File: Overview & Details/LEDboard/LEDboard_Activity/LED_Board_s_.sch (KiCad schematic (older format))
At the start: 6 parts, among them J1 Conn_01x04

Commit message: Create LEDboard schematic
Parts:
- added D10, D11, D12, D13, D14, D15, D16, D17, D18, D19, D2, D20, D21, D22, D23, D24, D25, D26, D27, D28, D29, D3, D30, D31, D32, D33, D34, D35, D36, D37, D38, D39, D4, D40, D41, D42, D43, D44, D45, D46, D47, D48, D5, D6, D7, D8, D9: APA102-2020, LED_SMD:LED-APA102-2020, symbol LED:APA102-2020
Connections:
- wire segments 9 -> 125
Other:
- note added: "NC"
- note removed: "n/c"

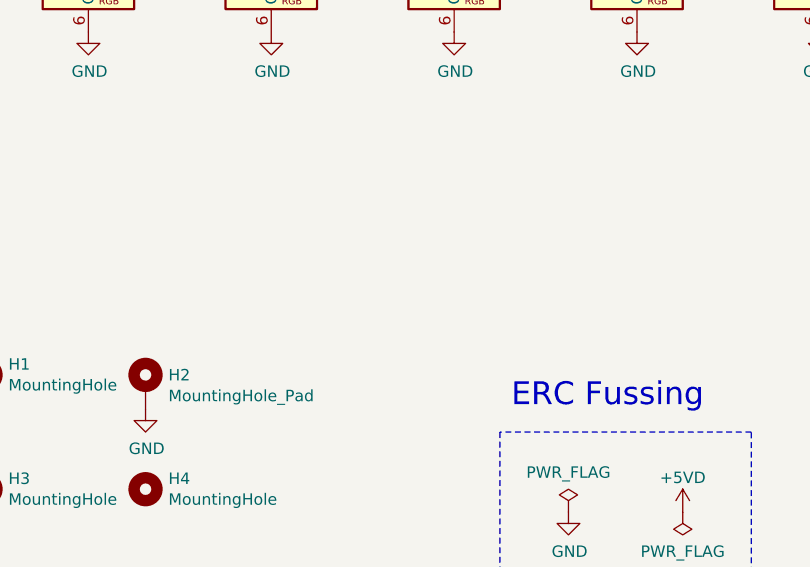
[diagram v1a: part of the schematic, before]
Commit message: add fiducials
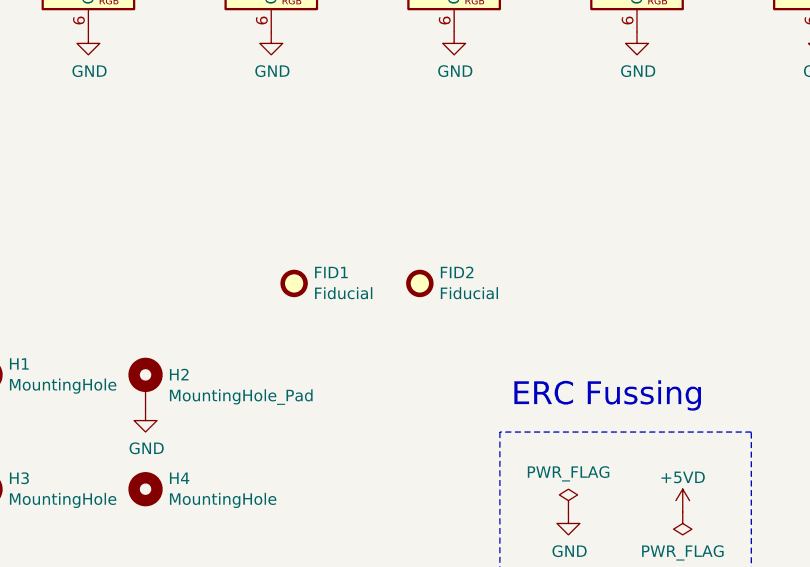
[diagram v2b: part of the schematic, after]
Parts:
- added FID1, FID2: Fiducial, Fiducial:Fiducial_0.5mm_Mask1mm, symbol Mechanical:Fiducial
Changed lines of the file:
@@
 Wire Wire Line
 	2200 6100 2700 6100
+$Comp
+L Mechanical:Fiducial FID1
+U 1 1 5EBD12B6
+P 10200 9100
+F 0 "FID1" H 10285 9146 50  0000 L CNN
+F 1 "Fiducial" H 10285 9055 50  0000 L CNN
+F 2 "Fiducial:Fiducial_0.5mm_Mask1mm" H 10200 9100 50  0001 C CNN
+F 3 "~" H 10200 9100 50  0001 C CNN
+	1    10200 9100
+	1    0    0    -1
+$EndComp
+$Comp
+L Mechanical:Fiducial FID2
+U 1 1 5EBD2ECE
+P 10750 9100
+F 0 "FID2" H 10835 9146 50  0000 L CNN
+F 1 "Fiducial" H 10835 9055 50  0000 L CNN
+F 2 "Fiducial:Fiducial_0.5mm_Mask1mm" H 10750 9100 50  0001 C CNN
+F 3 "~" H 10750 9100 50  0001 C CNN
+	1    10750 9100
+	1    0    0    -1
+$EndComp
 $EndSCHEMATC
